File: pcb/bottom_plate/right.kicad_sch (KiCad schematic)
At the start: 20 parts

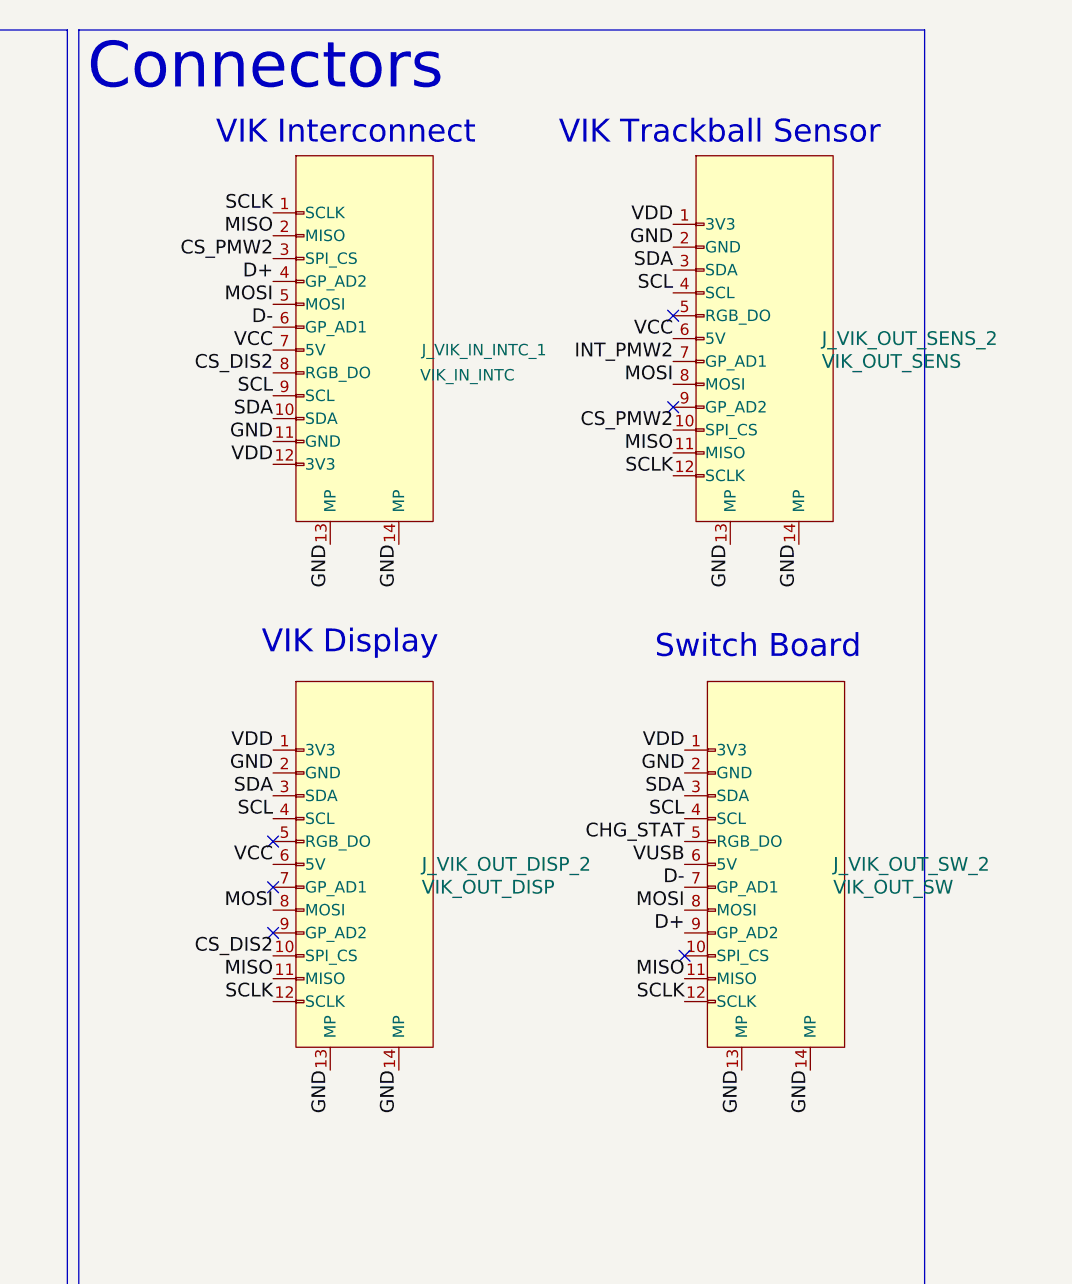
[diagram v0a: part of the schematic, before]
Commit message: Update KiCAD projects to use new library locations.
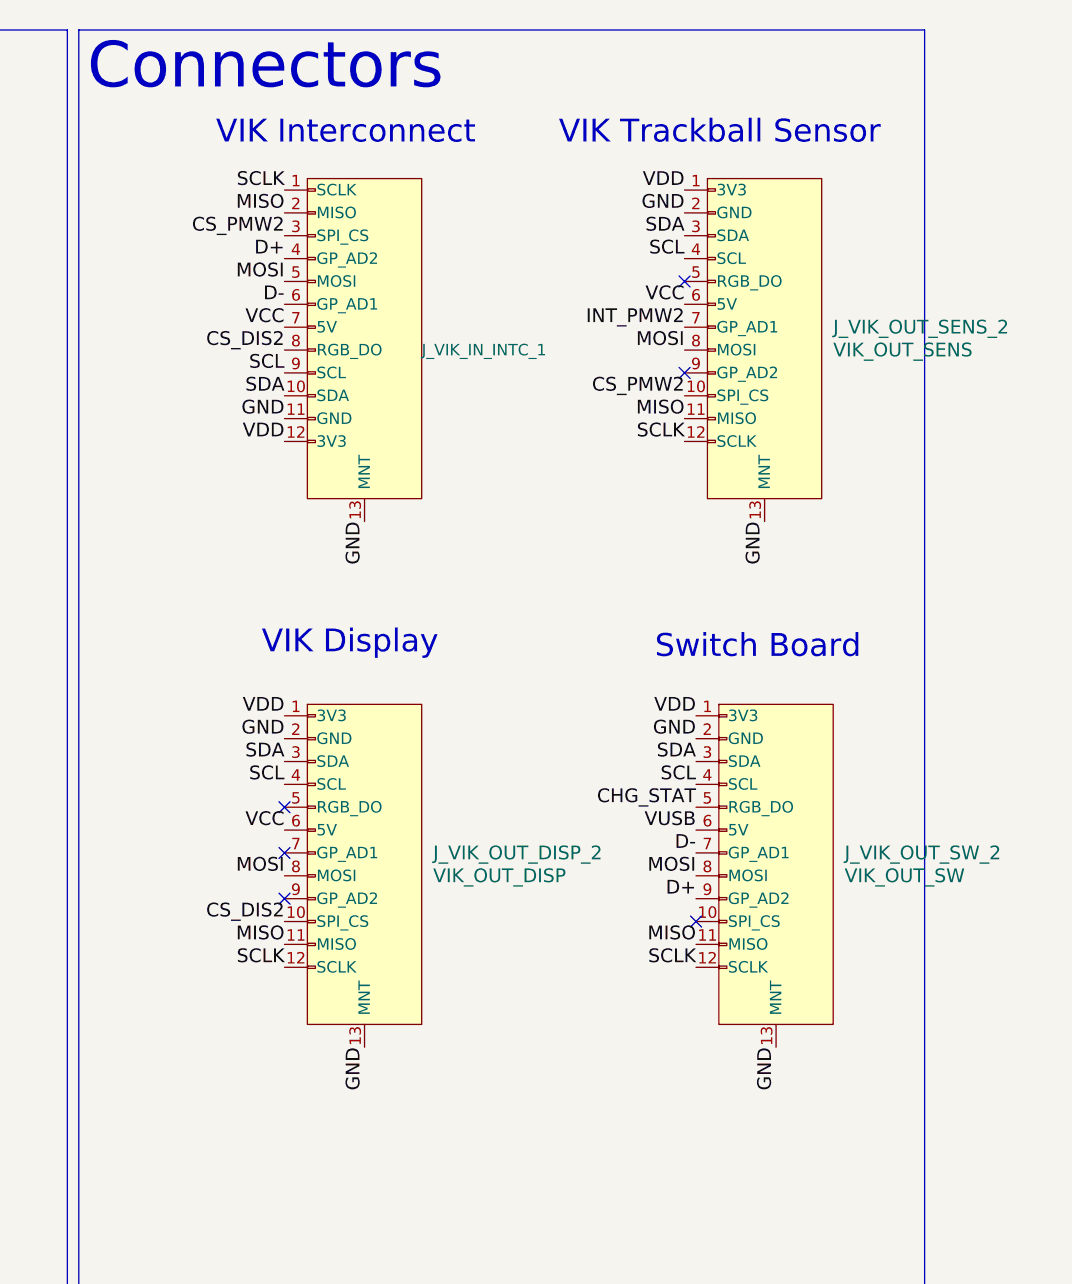
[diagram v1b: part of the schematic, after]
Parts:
- J_VIK_IN_INTC_1: footprint vik:vik-module-connector-horizontal -> footprints:vik-module-connector-horizontal
- J_VIK_OUT_DISP_2, J_VIK_OUT_SENS_2, J_VIK_OUT_SW_2: footprint vik:vik-keyboard-connector-horizontal -> footprints:vik-keyboard-connector-horizontal
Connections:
- net GND: no longer J_VIK_IN_INTC_1.14 (MP), J_VIK_OUT_DISP_2.14 (MP), J_VIK_OUT_SENS_2.14 (MP), J_VIK_OUT_SW_2.14 (MP)
